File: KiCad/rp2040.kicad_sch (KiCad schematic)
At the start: 28 parts, among them U4 AP2112K-3.3, U5 GD25Q16xS, U6 RP2040, Y1 XYDBPCNANF-12MHZ

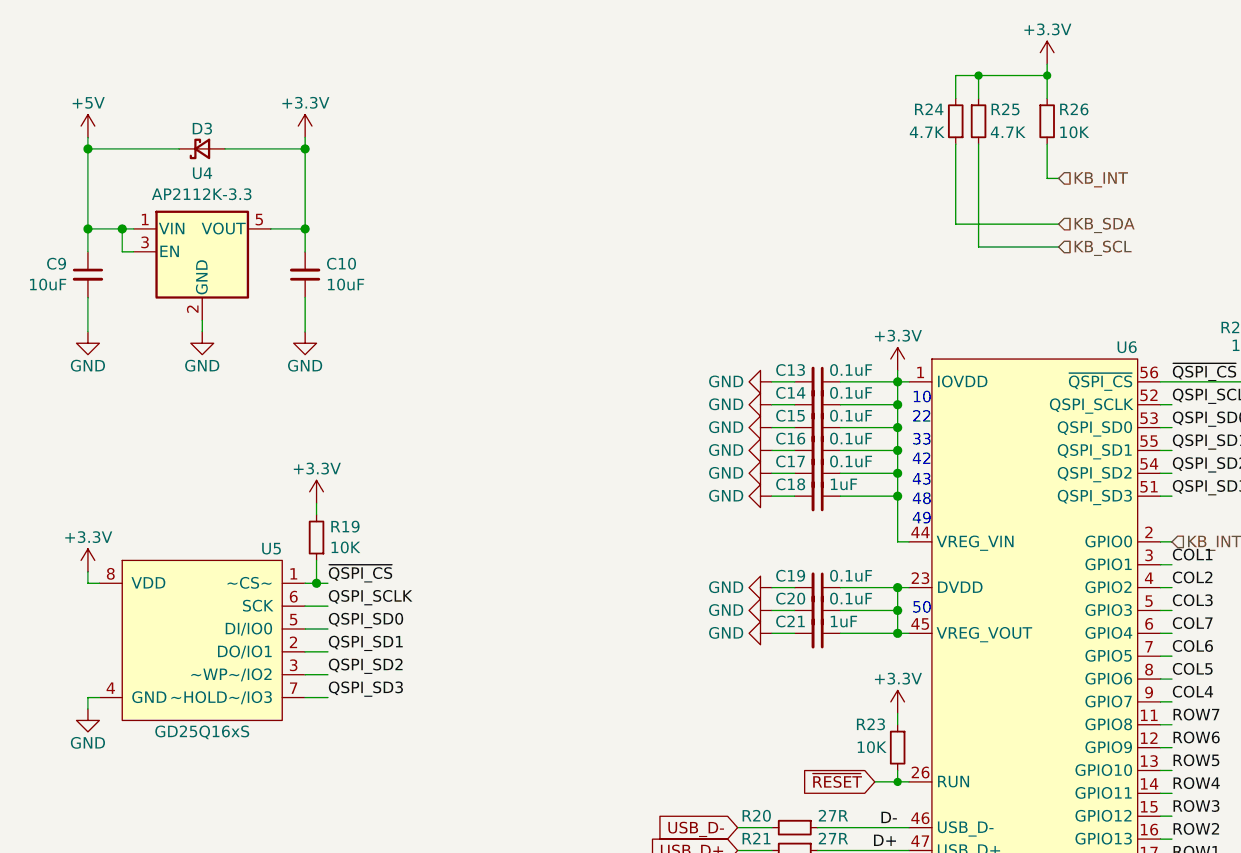
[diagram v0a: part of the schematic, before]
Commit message: Moved 4 layers to 2 layers with ground fill
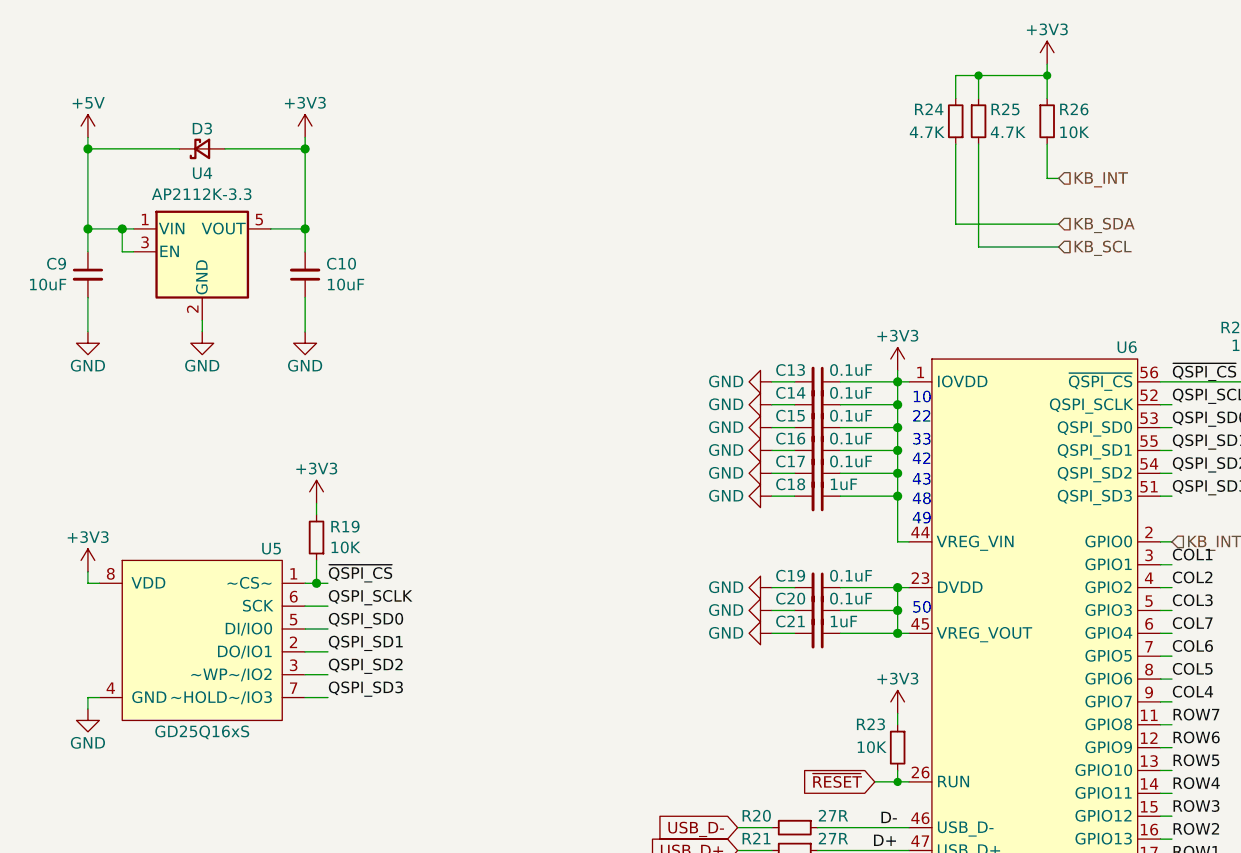
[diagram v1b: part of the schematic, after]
